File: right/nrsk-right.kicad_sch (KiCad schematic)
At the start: 137 parts, among them J1 PJ-320D, J2 USB-C, J3 OLED 128x32, SW1 71, SW10 8, SW11 9, SW12 0, SW13 -, SW14 =, SW15 Backspace, SW16 75, SW17 Y, SW18 U, SW19 I, SW2 F7, SW20 O, SW21 P, SW22 [, SW23 ], SW24 \, SW25 77, SW26 H, SW27 J, SW28 K, SW29 L, SW3 F8, SW30 ;, SW31 ', SW32 Enter, SW33 79, SW34 N, SW35 M, SW36 ,, SW37 ., SW38 /, SW39 ↑, SW4 F9, SW40 fn, SW41 81, SW42 Space, SW43 Space, SW44 Cmd, SW45 Opt, SW46 ←, SW47 ↓, SW48 →, SW5 F10, SW6 F11, SW7 F12, SW8 73, SW9 7, U1 RP2040, U2 USBLC6-2SC6, U4 AP2112K-3.3, U5 W25Q128JVS, Y1 12MHz

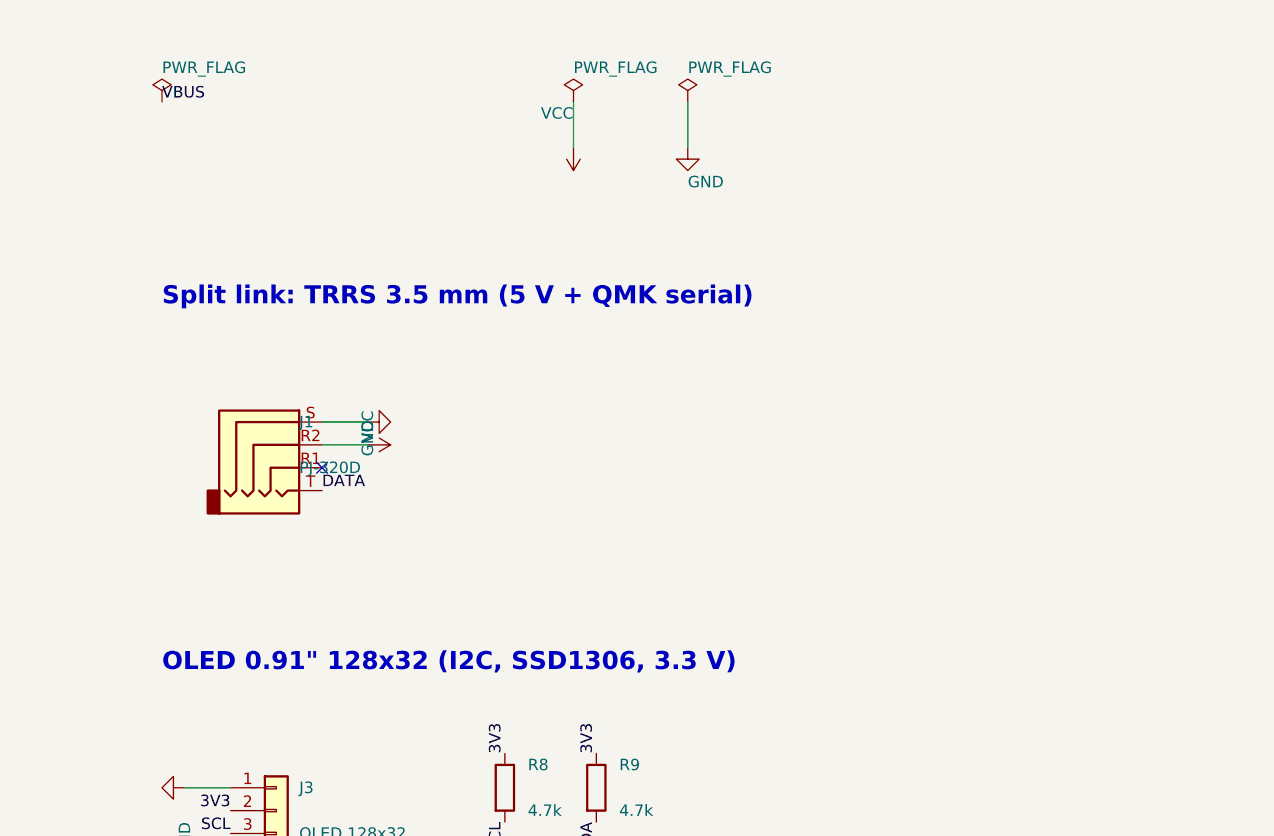
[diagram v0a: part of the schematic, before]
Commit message: Split link over USB-C instead of TRRS, so both port openings line up
The TRRS jack (PJ-320D) hung 5.0 mm under the PCB with its axis 2.5 mm down,
while the USB-C shell's axis is 1.63 mm down, so the two openings in the back
wall sat at different heights. The link now uses a second HRO TYPE-C-31-M-12:
same part, same height, same rounded slot.

- J1 is a USB-C receptacle: VBUS = VCC, D+ (A6/B6) = DATA (GP1), GND; D- and
  CC open, so a host or charger plugged in by mistake keeps VBUS off.
- PCB / case / JLC / BOM generators: the 'trrs' connector kind becomes 'link'
  and is handled like the host USB-C; PJ-320D footprint, model and JLC fix go.
- BOM: 4 USB-C receptacles, a C-C data cable for the link; one fewer
  Extended JLC part (9).
- Docs: README, ordering, pre-order checklist, thumbwheel check, assembly
  guide updated (pinout, which port is which, data cable required).
- Rebuilt: schematics, PCBs (0 unconnected, 0 parity issues, 4 silk warnings
  per side), fab outputs, case, BOM, JLC files, KiCad doc images.

Co-Authored-By: Claude Opus 5.5 <noreply@anthropic.com>
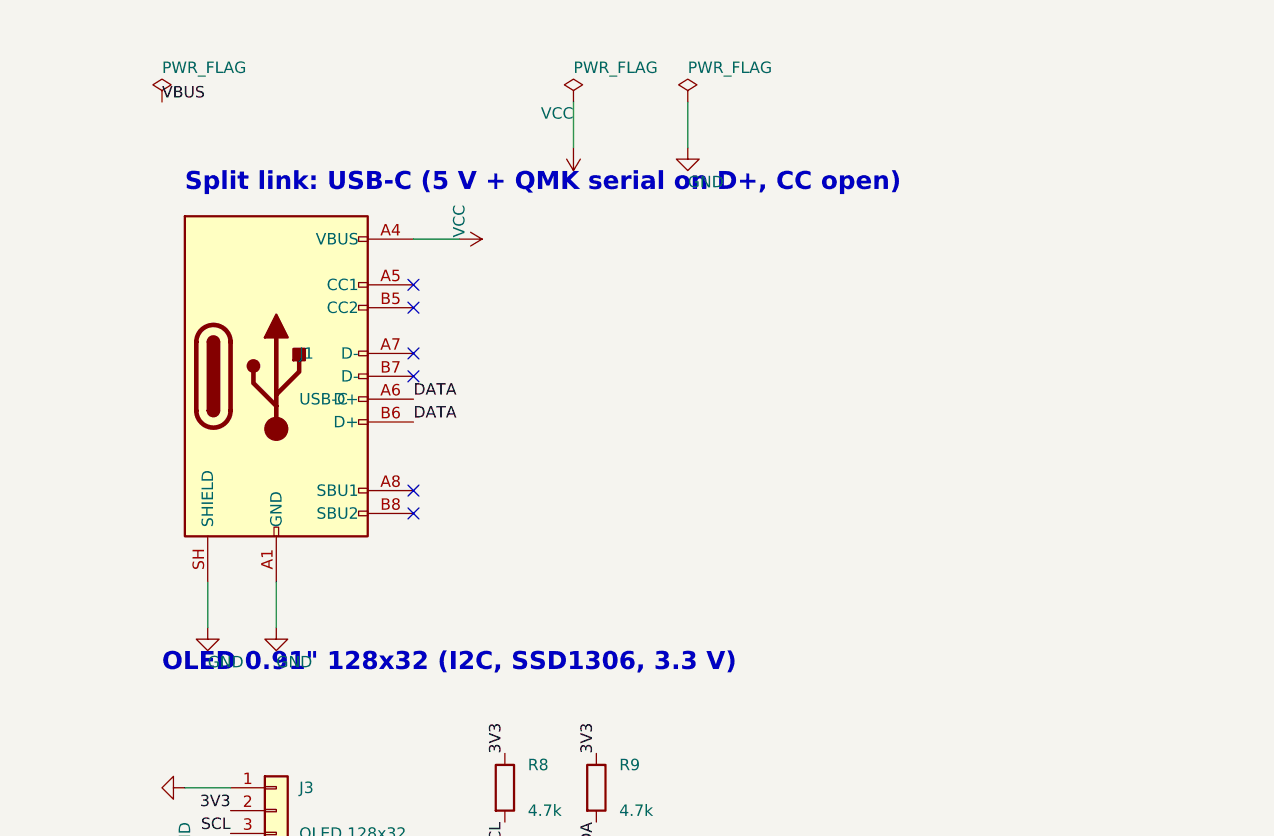
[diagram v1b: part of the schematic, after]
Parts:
- J1: value PJ-320D -> USB-C; footprint Connector_Audio:Jack_3.5mm_PJ320D_Horizontal -> Connector_USB:USB_C_Receptacle_HRO_TYPE-C-31-M-12; symbol Connector_Audio:AudioJack4 -> Connector:USB_C_Receptacle_USB2.0_16P
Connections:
- net DATA: now also J1.A6 (D+), J1.B6 (D+); no longer J1.T
- net GND: now also J1.A1 (GND), J1.A12 (GND), J1.B1 (GND), J1.B12 (GND), J1.SH (SHIELD); no longer J1.S
- net VCC: now also J1.A4 (VBUS), J1.A9 (VBUS), J1.B4 (VBUS), J1.B9 (VBUS); no longer J1.R2
- no-connect marks 16 -> 21
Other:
- note added: "Split link: USB-C (5 V + QMK serial on D+, CC open)"
- note removed: "Split link: TRRS 3.5 mm (5 V + QMK serial)"
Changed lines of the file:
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@@
 	  (instances (project "nrsk-right" (path "/ed20d8a8-6cf2-52f9-90d9-bd3277b2df44" (reference "#PWR040") (unit 1))))
 	)
-	(text "Split link: TRRS 3.5 mm (5 V + QMK serial)" (exclude_from_sim no) (at 330.20 160.02 0) (effects (font (size 2.0 2.0) (bold yes)) (justify left bottom)))
-	(symbol (lib_id "Connector_Audio:AudioJack4") (at 342.90 175.26 0) (unit 1) (exclude_from_sim no) (in_bom yes) (on_board yes) (dnp no)
-	  (property "Reference" "J1" (at 345.44 172.72 0) (effects (font (size 1.27 1.27)) (justify left)))
-	  (property "Value" "PJ-320D" (at 345.44 177.80 0) (effects (font (size 1.27 1.27)) (justify left)))
-	  (property "Footprint" "Connector_Audio:Jack_3.5mm_PJ320D_Horizontal" (at 342.90 175.26 0) (effects (font (size 1.27 1.27)) (hide yes)))
-	  (property "Datasheet" "" (at 342.90 175.26 0) (effects (font (size 1.27 1.27)) (hide yes)))
-	  (pin "R1")
-	  (pin "R2")
-	  (pin "S")
-	  (pin "T")
+	(text "Split link: USB-C (5 V + QMK serial on D+, CC open)" (exclude_from_sim no) (at 332.74 147.32 0) (effects (font (size 2.0 2.0) (bold yes)) (justify left bottom)))
+	(symbol (lib_id "Connector:USB_C_Receptacle_USB2.0_16P") (at 342.90 167.64 0) (unit 1) (exclude_from_sim no) (in_bom yes) (on_board yes) (dnp no)
+	  (property "Reference" "J1" (at 345.44 165.10 0) (effects (font (size 1.27 1.27)) (justify left)))
+	  (property "Value" "USB-C" (at 345.44 170.18 0) (effects (font (size 1.27 1.27)) (justify left)))
+	  (property "Footprint" "Connector_USB:USB_C_Receptacle_HRO_TYPE-C-31-M-12" (at 342.90 167.64 0) (effects (font (size 1.27 1.27)) (hide yes)))
+	  (property "Datasheet" "" (at 342.90 167.64 0) (effects (font (size 1.27 1.27)) (hide yes)))
+	  (pin "A1")
+	  (pin "A4")
+	  (pin "A5")
+	  (pin "A6")
+	  (pin "A7")
+	  (pin "A8")
+	  (pin "A9")
+	  (pin "A12")
+	  (pin "B1")
+	  (pin "B4")
+	  (pin "B5")
+	  (pin "B6")
+	  (pin "B7")
+	  (pin "B8")
+	  (pin "B9")
+	  (pin "B12")
+	  (pin "SH")
 	  (instances (project "nrsk-right" (path "/ed20d8a8-6cf2-52f9-90d9-bd3277b2df44" (reference "J1") (unit 1))))
 	)
-	(no_connect (at 347.98 177.80))
-	(wire (pts (xy 347.98 175.26) (xy 353.06 175.26)) (stroke (width 0) (type default)))
-	(symbol (lib_id "power:VCC") (at 353.06 175.26 270) (unit 1) (exclude_from_sim no) (in_bom no) (on_board no) (dnp no)
-	  (property "Reference" "#PWR041" (at 353.06 175.26 0) (effects (font (size 1.27 1.27)) (justify left) (hide yes)))
-	  (property "Value" "VCC" (at 353.06 171.45 0) (effects (font (size 1.27 1.27)) (justify left)))
-	  (property "Footprint" "" (at 353.06 175.26 0) (effects (font (size 1.27 1.27)) (hide yes)))
-	  (property "Datasheet" "" (at 353.06 175.26 0) (effects (font (size 1.27 1.27)) (hide yes)))
+	(wire (pts (xy 342.90 190.50) (xy 342.90 195.58)) (stroke (width 0) (type default)))
+	(symbol (lib_id "power:GND") (at 342.90 195.58 0) (unit 1) (exclude_from_sim no) (in_bom no) (on_board no) (dnp no)
+	  (property "Reference" "#PWR041" (at 342.90 195.58 0) (effects (font (size 1.27 1.27)) (justify left) (hide yes)))
+	  (property "Value" "GND" (at 342.90 199.39 0) (effects (font (size 1.27 1.27)) (justify left)))
+	  (property "Footprint" "" (at 342.90 195.58 0) (effects (font (size 1.27 1.27)) (hide yes)))
+	  (property "Datasheet" "" (at 342.90 195.58 0) (effects (font (size 1.27 1.27)) (hide yes)))
 	  (pin "1")
 	  (instances (project "nrsk-right" (path "/ed20d8a8-6cf2-52f9-90d9-bd3277b2df44" (reference "#PWR041") (unit 1))))
 	)
-	(wire (pts (xy 347.98 172.72) (xy 353.06 172.72)) (stroke (width 0) (type default)))
-	(symbol (lib_id "power:GND") (at 353.06 172.72 90) (unit 1) (exclude_from_sim no) (in_bom no) (on_board no) (dnp no)
-	  (property "Reference" "#PWR042" (at 353.06 172.72 0) (effects (font (size 1.27 1.27)) (justify left) (hide yes)))
-	  (property "Value" "GND" (at 353.06 176.53 0) (effects (font (size 1.27 1.27)) (justify left)))
-	  (property "Footprint" "" (at 353.06 172.72 0) (effects (font (size 1.27 1.27)) (hide yes)))
-	  (property "Datasheet" "" (at 353.06 172.72 0) (effects (font (size 1.27 1.27)) (hide yes)))
+	(wire (pts (xy 358.14 152.40) (xy 363.22 152.40)) (stroke (width 0) (type default)))
+	(symbol (lib_id "power:VCC") (at 363.22 152.40 270) (unit 1) (exclude_from_sim no) (in_bom no) (on_board no) (dnp no)
+	  (property "Reference" "#PWR042" (at 363.22 152.40 0) (effects (font (size 1.27 1.27)) (justify left) (hide yes)))
+	  (property "Value" "VCC" (at 363.22 148.59 0) (effects (font (size 1.27 1.27)) (justify left)))
+	  (property "Footprint" "" (at 363.22 152.40 0) (effects (font (size 1.27 1.27)) (hide yes)))
+	  (property "Datasheet" "" (at 363.22 152.40 0) (effects (font (size 1.27 1.27)) (hide yes)))
 	  (pin "1")
 	  (instances (project "nrsk-right" (path "/ed20d8a8-6cf2-52f9-90d9-bd3277b2df44" (reference "#PWR042") (unit 1))))
 	)
-	(label "DATA" (at 347.98 180.34 0) (effects (font (size 1.27 1.27)) (justify left bottom)))
+	(no_connect (at 358.14 157.48))
+	(label "DATA" (at 358.14 170.18 0) (effects (font (size 1.27 1.27)) (justify left bottom)))
+	(no_connect (at 358.14 165.10))
+	(no_connect (at 358.14 180.34))
+	(no_connect (at 358.14 160.02))
+	(label "DATA" (at 358.14 172.72 0) (effects (font (size 1.27 1.27)) (justify left bottom)))
+	(no_connect (at 358.14 167.64))
+	(no_connect (at 358.14 182.88))
+	(wire (pts (xy 335.28 190.50) (xy 335.28 195.58)) (stroke (width 0) (type default)))
+	(symbol (lib_id "power:GND") (at 335.28 195.58 0) (unit 1) (exclude_from_sim no) (in_bom no) (on_board no) (dnp no)
+	  (property "Reference" "#PWR043" (at 335.28 195.58 0) (effects (font (size 1.27 1.27)) (justify left) (hide yes)))
+	  (property "Value" "GND" (at 335.28 199.39 0) (effects (font (size 1.27 1.27)) (justify left)))
+	  (property "Footprint" "" (at 335.28 195.58 0) (effects (font (size 1.27 1.27)) (hide yes)))
+	  (property "Datasheet" "" (at 335.28 195.58 0) (effects (font (size 1.27 1.27)) (hide yes)))
+	  (pin "1")
+	  (instances (project "nrsk-right" (path "/ed20d8a8-6cf2-52f9-90d9-bd3277b2df44" (reference "#PWR043") (unit 1))))
+	)
 	(text "OLED 0.91\" 128x32 (I2C, SSD1306, 3.3 V)" (exclude_from_sim no) (at 330.20 200.66 0) (effects (font (size 2.0 2.0) (bold yes)) (justify left bottom)))
 	(symbol (lib_id "Connector_Generic:Conn_01x04") (at 342.90 215.90 0) (unit 1) (exclude_from_sim no) (in_bom yes) (on_board yes) (dnp no)
@@
 	(wire (pts (xy 337.82 213.36) (xy 332.74 213.36)) (stroke (width 0) (type default)))
 	(symbol (lib_id "power:GND") (at 332.74 213.36 270) (unit 1) (exclude_from_sim no) (in_bom no) (on_board no) (dnp no)
-	  (property "Reference" "#PWR043" (at 332.74 213.36 0) (effects (font (size 1.27 1.27)) (justify left) (hide yes)))
+	  (property "Reference" "#PWR044" (at 332.74 213.36 0) (effects (font (size 1.27 1.27)) (justify left) (hide yes)))
 	  (property "Value" "GND" (at 332.74 217.17 0) (effects (font (size 1.27 1.27)) (justify left)))
 	  (property "Footprint" "" (at 332.74 213.36 0) (effects (font (size 1.27 1.27)) (hide yes)))
 	  (property "Datasheet" "" (at 332.74 213.36 0) (effects (font (size 1.27 1.27)) (hide yes)))
 	  (pin "1")
-	  (instances (project "nrsk-right" (path "/ed20d8a8-6cf2-52f9-90d9-bd3277b2df44" (reference "#PWR043") (unit 1))))
+	  (instances (project "nrsk-right" (path "/ed20d8a8-6cf2-52f9-90d9-bd3277b2df44" (reference "#PWR044") (unit 1))))
 	)
 	(label "3V3" (at 337.82 215.90 180) (effects (font (size 1.27 1.27)) (justify right bottom)))
@@
 	(wire (pts (xy 335.28 254.00) (xy 330.20 254.00)) (stroke (width 0) (type default)))
 	(symbol (lib_id "power:GND") (at 330.20 254.00 270) (unit 1) (exclude_from_sim no) (in_bom no) (on_board no) (dnp no)
-	  (property "Reference" "#PWR044" (at 330.20 254.00 0) (effects (font (size 1.27 1.27)) (justify left) (hide yes)))
+	  (property "Reference" "#PWR045" (at 330.20 254.00 0) (effects (font (size 1.27 1.27)) (justify left) (hide yes)))
 	  (property "Value" "GND" (at 330.20 257.81 0) (effects (font (size 1.27 1.27)) (justify left)))
 	  (property "Footprint" "" (at 330.20 254.00 0) (effects (font (size 1.27 1.27)) (hide yes)))
 	  (property "Datasheet" "" (at 330.20 254.00 0) (effects (font (size 1.27 1.27)) (hide yes)))
 	  (pin "1")
-	  (instances (project "nrsk-right" (path "/ed20d8a8-6cf2-52f9-90d9-bd3277b2df44" (reference "#PWR044") (unit 1))))
+	  (instances (project "nrsk-right" (path "/ed20d8a8-6cf2-52f9-90d9-bd3277b2df44" (reference "#PWR045") (unit 1))))
 	)
 	(sheet_instances (path "/" (page "1")))
